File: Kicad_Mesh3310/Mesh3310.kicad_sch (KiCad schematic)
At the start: 16 parts, among them J1 USB device, SW2 "OK"

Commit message: Backing up work
Backup work for today
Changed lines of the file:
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@@
-		)
-	)
-	(label "P0.27_DSP_MOSI"
-		(at 41.91 96.52 0)
-		(effects
-			(font
-				(size 1.27 1.27)
-			)
-			(justify left bottom)
 		)
 	)
@@
 		)
 	)
-	(label "P1.01_ROW_4"
+	(label "P1.04_ROW_4"
 		(at 125.73 49.53 180)
 		(effects

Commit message: Backup work
Adding some extra pads
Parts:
- TP10, TP11, TP12, TP9: footprint TestPoint:TestPoint_Pad_D1.5mm -> TestPoint:TestPoint_Pad_D2.0mm
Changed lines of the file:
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@@
 			)
 		)
-		(property "Footprint" "TestPoint:TestPoint_Pad_D1.5mm"
+		(property "Footprint" "TestPoint:TestPoint_Pad_D2.0mm"
 			(at 154.94 109.22 0)
 			(effects
@@
 			)
 		)
-		(property "Footprint" "TestPoint:TestPoint_Pad_D1.5mm"
+		(property "Footprint" "TestPoint:TestPoint_Pad_D2.0mm"
 			(at 170.18 87.63 0)
 			(effects
@@
 			)
 		)
-		(property "Footprint" "TestPoint:TestPoint_Pad_D1.5mm"
+		(property "Footprint" "TestPoint:TestPoint_Pad_D2.0mm"
 			(at 157.48 109.22 0)
 			(effects
@@
 			)
 		)
-		(property "Footprint" "TestPoint:TestPoint_Pad_D1.5mm"
+		(property "Footprint" "TestPoint:TestPoint_Pad_D2.0mm"
 			(at 160.02 87.63 0)
 			(effects

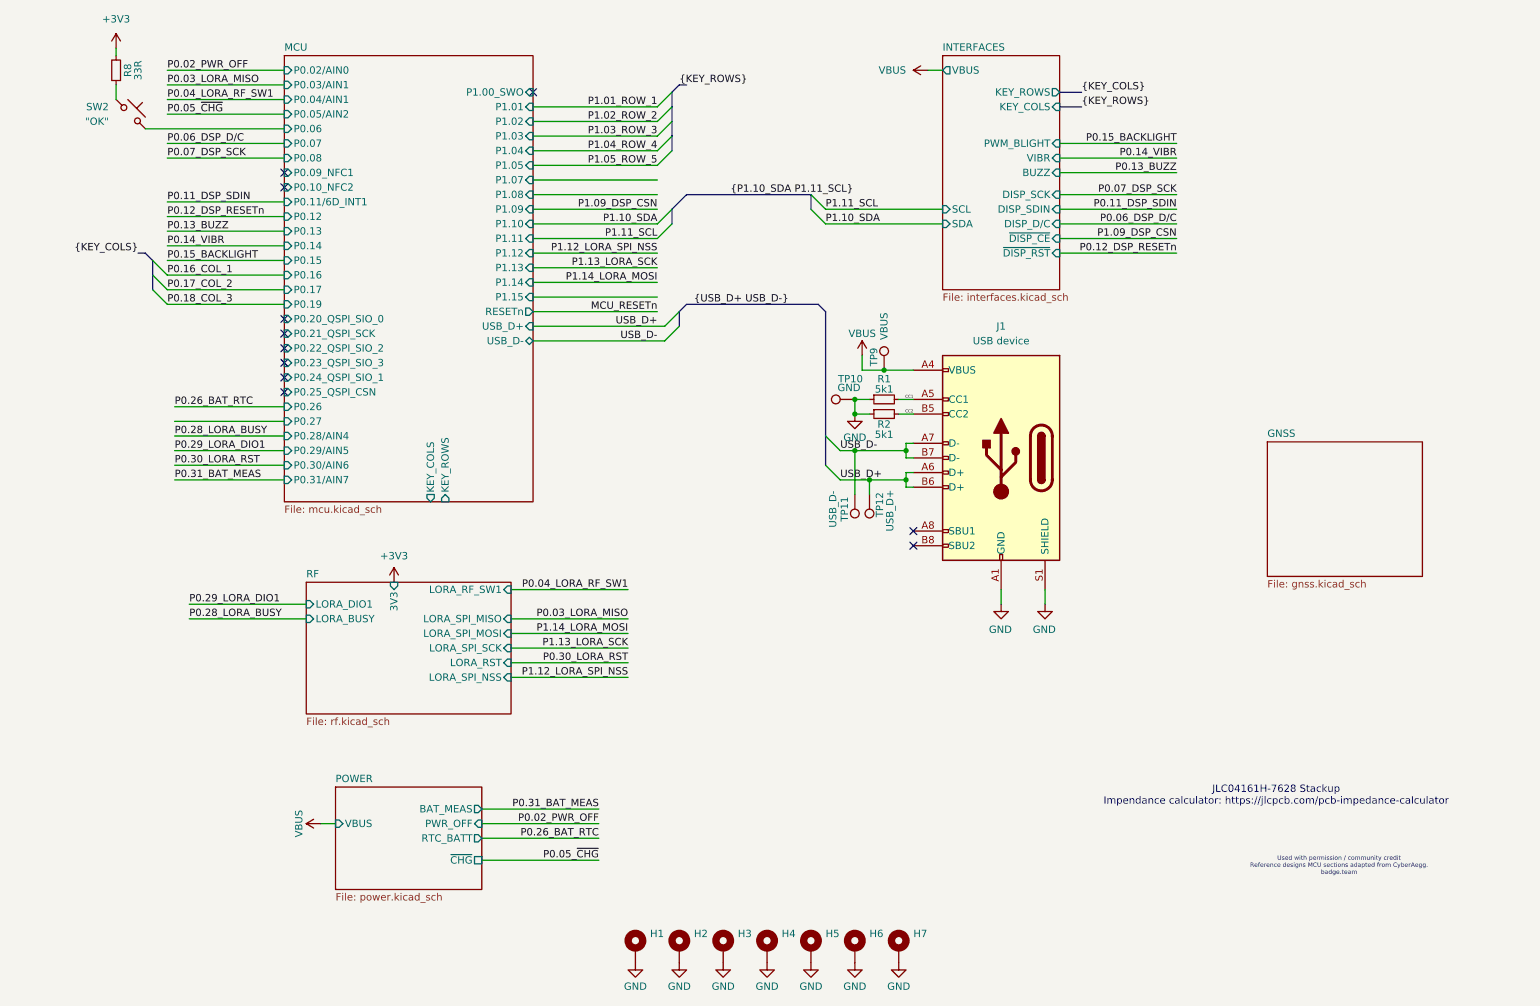
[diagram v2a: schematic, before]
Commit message: Schematic changes
Adding gsm module , interfaces : mic+earspeaker
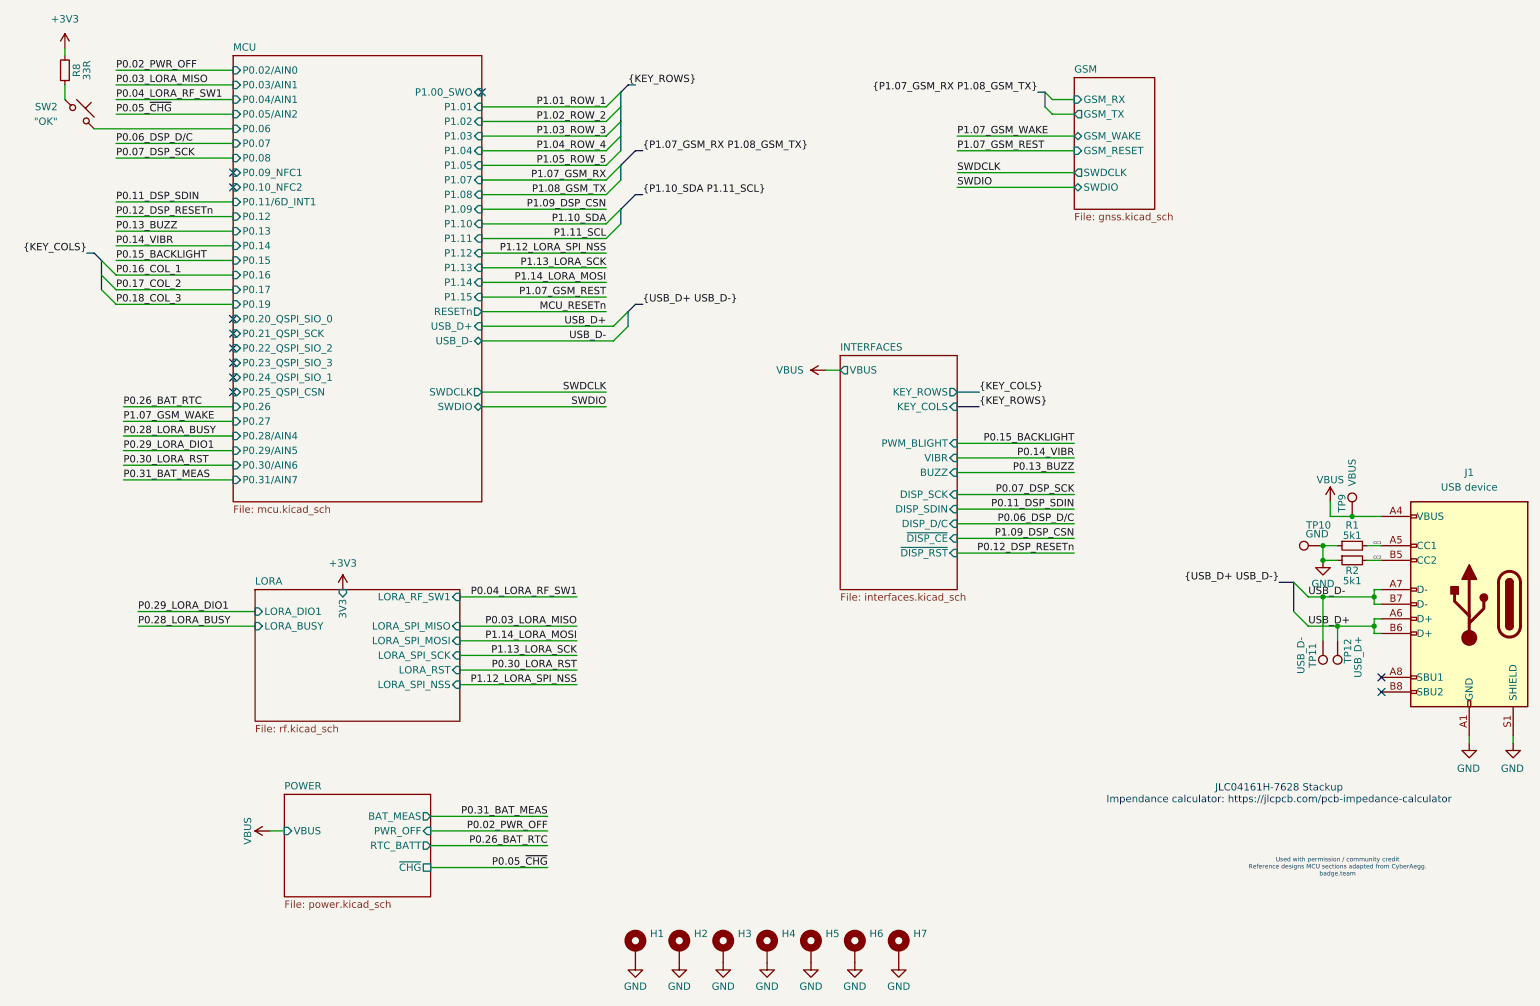
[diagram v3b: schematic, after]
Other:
- sheet GNSS renamed GSM
- sheet RF renamed LORA
- sheet GSM ports: added GSM_RESET, GSM_RX, GSM_TX, GSM_WAKE, SWDCLK, SWDIO; removed none
- sheet INTERFACES ports: added none; removed SCL, SDA
- sheet MCU ports: added SWDCLK, SWDIO; removed KEY_COLS, KEY_ROWS
- moved on the sheet: J1, R1, R2, R8, SW2, TP10, TP11, TP12, TP9
